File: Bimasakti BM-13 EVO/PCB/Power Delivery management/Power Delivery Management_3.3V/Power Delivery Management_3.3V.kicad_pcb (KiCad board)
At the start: 2 copper layers, 42.4 x 42.4 mm, 27 parts, among them J1 +12V In, J2 Conn_01x03_Socket, J3 Slow Start

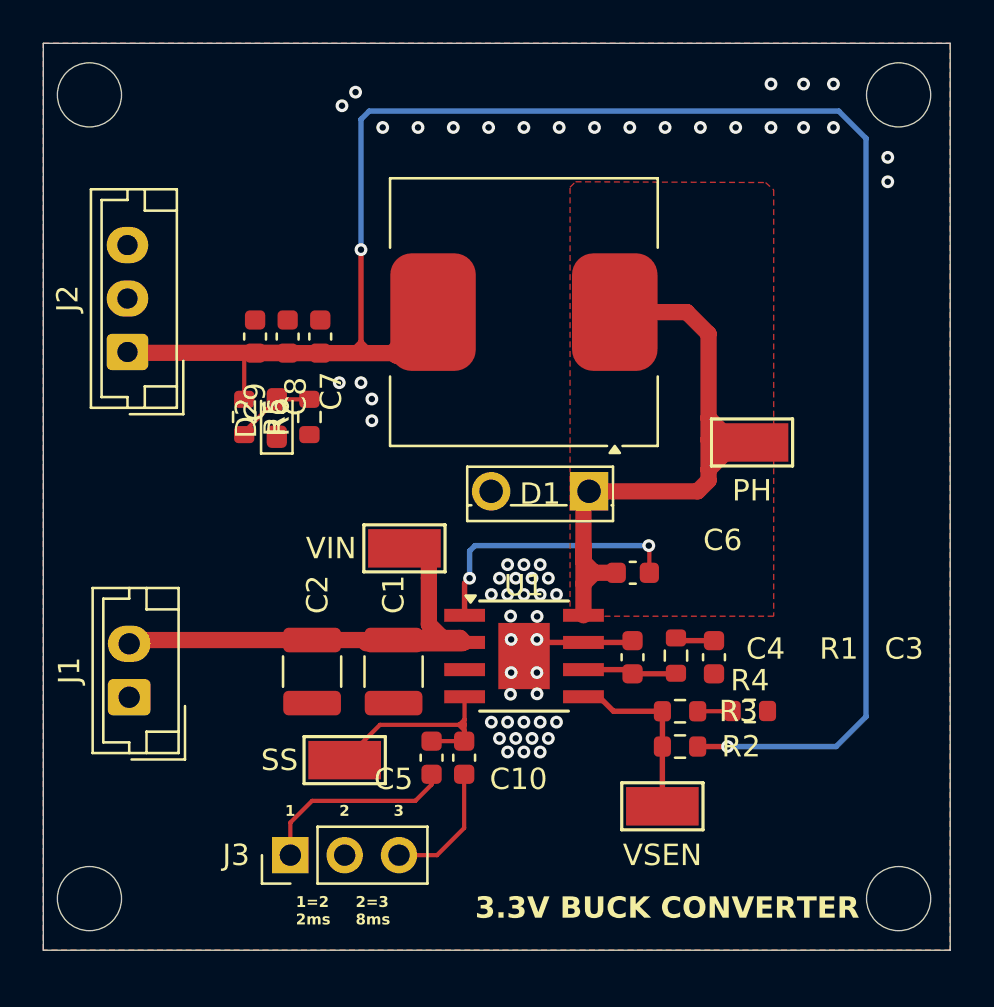
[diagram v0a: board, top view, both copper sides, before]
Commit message: ganti value dan layout
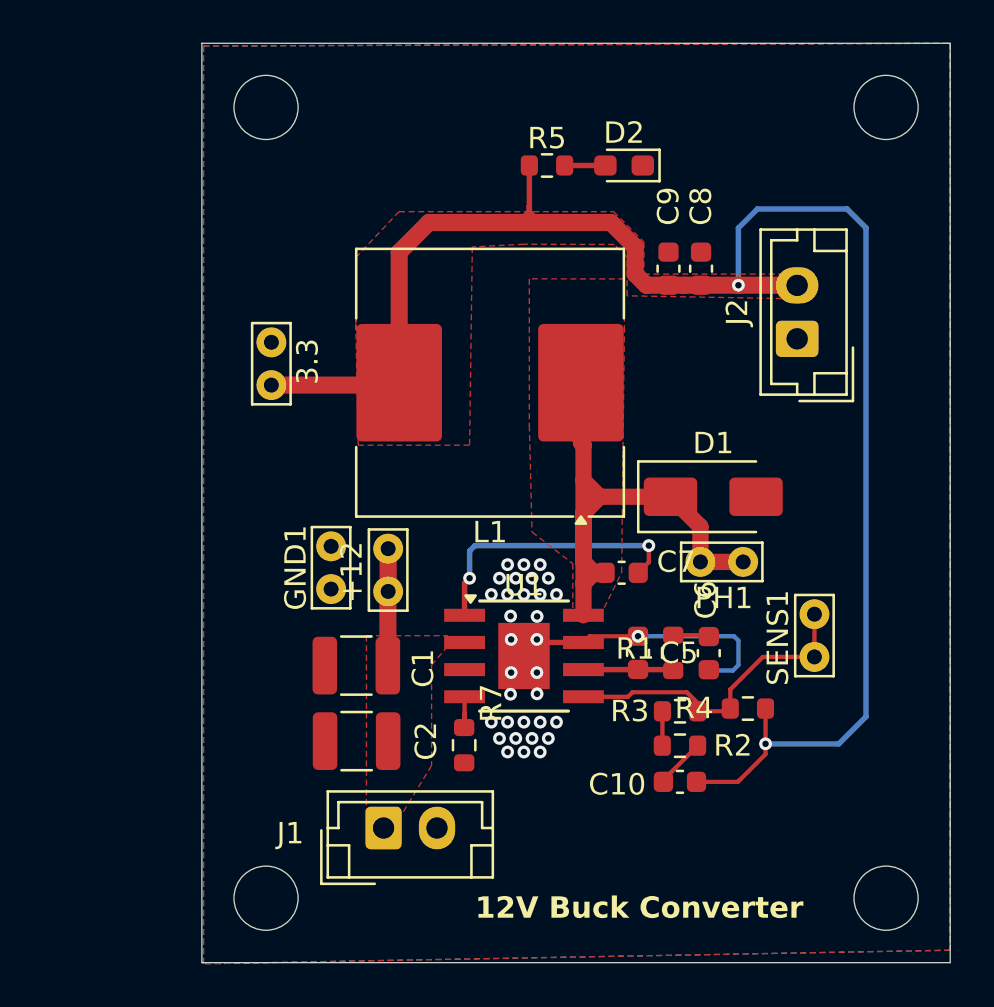
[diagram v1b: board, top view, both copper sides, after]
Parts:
- removed C3: 1nF, Capacitor_SMD:C_0603_1608Metric
- removed C4: 10pF, Capacitor_SMD:C_0603_1608Metric
- removed J3: Slow Start, Connector_PinHeader_2.54mm:PinHeader_1x03_P2.54mm_Vertical
- removed PH, SS, VIN, VSEN: TestPoint, TestPoint:TestPoint_Keystone_5015_Micro-Minature
- removed R6: 1.5k, Resistor_SMD:R_0603_1608Metric
- added +12: TestPoint, TestPoint:TestPoint_Bridge_Pitch2.0mm_Drill0.7mm, F.Cu at (49.5, 53.0)
- added 3.3: TestPoint, TestPoint:TestPoint_Bridge_Pitch2.0mm_Drill0.7mm, F.Cu at (44.1, 45.3)
- added GND1: TestPoint, TestPoint:TestPoint_Bridge_Pitch2.0mm_Drill0.7mm, F.Cu at (46.9, 54.9)
- added PH1: TestPoint, TestPoint:TestPoint_Bridge_Pitch2.0mm_Drill0.7mm, F.Cu at (64.1, 53.6)
- added R7: 56k, Resistor_SMD:R_0603_1608Metric, F.Cu at (53.1, 62.2)
- added SENS1: TestPoint, TestPoint:TestPoint_Bridge_Pitch2.0mm_Drill0.7mm, F.Cu at (69.5, 56.0)
- C10: value 20nF -> 47uF
- C2: value 22uF -> 100uF
- C5: value 5nF -> 180pF
- C6: value 100nF -> 5.1nF
- C7: value 47uF -> 100nF
- D1: footprint Package_TO_SOT_THT:TO-251-2_Vertical -> Diode_SMD:D_SMA
- J2: value Conn_01x03_Socket -> 3.3V; footprint Connector_JST:JST_EH_B3B-EH-A_1x03_P2.50mm_Vertical -> Connector_JST:JST_EH_B2B-EH-A_1x02_P2.50mm_Vertical
- L1: value 12uH -> 4.7uH
- R2: value 10k -> 220
- R3: value 1.5k -> 3k
- R4: value 390 -> 10k
- R5: value 1k -> 220
- moved J2 31.3 mm to (68.7, 43.2)
- moved D2 20.1 mm to (60.6, 35.1), turned to 180 degrees
- moved C8 19.6 mm to (64.2, 39.9)
- moved C9 19.6 mm to (62.6, 39.9)
- moved R5 18.4 mm to (57.0, 35.1), turned to 0 degrees
- moved C7 17.9 mm to (60.5, 54.1), turned to 180 degrees
- moved J1 13.4 mm to (49.3, 66.0), turned to 0 degrees
- moved C5 10.8 mm to (61.2, 57.8)
- moved C10 10.2 mm to (63.2, 63.9), turned to 180 degrees
- moved D1 5.82 mm to (64.7, 50.5), turned to 0 degrees
- moved C6 5.17 mm to (64.5, 57.9), turned to -90 degrees
- moved C2 3.86 mm to (48.1, 62.0), turned to 180 degrees
- moved L1 3.66 mm to (54.3, 45.2)
- moved C1 1.76 mm to (48.0, 58.4), turned to 180 degrees
- moved R1 0.18 mm to (62.9, 57.8)
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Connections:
- C1 pad 1: (no net) -> +12V
- C1 pad 2: (no net) -> GND
- C10 pad 1: (no net) -> 3.3V
- C10 pad 2: (no net) -> GND
- C2 pad 1: (no net) -> +12V
- C2 pad 2: (no net) -> GND
- C5 pad 1: (no net) -> COMP
- C5 pad 2: (no net) -> GND
- C6 pad 1: (no net) -> Net-(C6-Pad1)
- C6 pad 2: (no net) -> GND
- C7 pad 1: (no net) -> BOOT
- C7 pad 2: (no net) -> PH
- C8 pad 1: (no net) -> 3.3V
- C8 pad 2: (no net) -> GND
- C9 pad 1: (no net) -> 3.3V
- C9 pad 2: (no net) -> GND
- D1 pad 1: (no net) -> PH
- D1 pad 2: (no net) -> GND
- J1 pad 1: (no net) -> +12V
- J1 pad 2: (no net) -> GND
- J2 pad 1: (no net) -> GND
- J2 pad 2: (no net) -> 3.3V
- L1 pad 1: (no net) -> PH
- L1 pad 2: (no net) -> 3.3V
- R1 pad 1: (no net) -> COMP
- R1 pad 2: (no net) -> Net-(C6-Pad1)
- R2 pad 1: (no net) -> Net-(R2-Pad1)
- R2 pad 2: (no net) -> GND
- R3 pad 1: (no net) -> Net-(R2-Pad1)
- R3 pad 2: (no net) -> VSENSE
- R4 pad 1: (no net) -> 3.3V
- R4 pad 2: (no net) -> VSENSE
- R5 pad 1: +5v -> 3.3V
- U1 pad 1: (no net) -> BOOT
- U1 pad 2: (no net) -> +12V
- U1 pad 3: (no net) -> unconnected-(U1-EN-Pad3)
- U1 pad 4: (no net) -> Net-(U1-SS)
- U1 pad 5: (no net) -> VSENSE
- U1 pad 6: (no net) -> COMP
- U1 pad 7: (no net) -> GND
- U1 pad 8: (no net) -> PH
- U1 pad 9: (no net) -> GND
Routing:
- net (no net): track 118.7 -> 0.00 mm, vias 59 -> 0
- net +5v: track 96.7 -> 0.00 mm, vias 2 -> 0
- net 3.3V: track 0.00 -> 81.1 mm, vias 0 -> 2
- net PH: track 0.00 -> 25.8 mm
- net VSENSE: track 0.00 -> 15.8 mm
- net GND: track 0.00 -> 14.9 mm, vias 0 -> 33
- net BOOT: track 0.00 -> 13.1 mm, vias 0 -> 2
- net +12V: track 0.00 -> 5.64 mm
- net COMP: track 0.00 -> 4.47 mm
- net Net-(D2-A): track 3.81 -> 1.91 mm
- net Net-(C6-Pad1): track 0.00 -> 1.69 mm
- net Net-(U1-SS): track 0.00 -> 1.68 mm
- net Net-(R2-Pad1): track 0.00 -> 1.61 mm
- added copper zone on F.Cu, net +12V
- added copper zone on F.Cu, net 3.3V
- added copper zone on B.Cu, net GND
- added copper zone on F.Cu, net GND
- added copper zone on F.Cu, net PH
- removed copper zone on B.Cu, net (none)
- removed copper zone on F.Cu, net (none)
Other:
- board size 42.4 x 42.4 mm -> 35 x 43 mm
- board text added: "12V Buck Converter"
- board text removed: "1"
- board text removed: "1=2 2ms"
- board text removed: "2"
- board text removed: "2=3 8ms"
- board text removed: "3"
- board text removed: "3.3V BUCK CONVERTER"
